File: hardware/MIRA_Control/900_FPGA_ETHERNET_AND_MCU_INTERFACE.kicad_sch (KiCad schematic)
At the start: 73 parts, among them J900 RJE71-188-1412, T900 H5007NLT, U500 XC7A200T-2FBG484I, U900 74LVC125APW, U901 74LVC125APW, U902 DP83867IRRGZR, U903 TLV75525PDBVR, U904 TPD2EUSB30DRTR, U905 TPD2EUSB30DRTR, U906 TPD2EUSB30DRTR, U907 TPD2EUSB30DRTR, Y900 ABM8-25.000MHZ-B2-T

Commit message: Add high-load schematic candidate with CORE sense and revised N15 supply
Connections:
- net VDD1P0 renamed PHY1V05
- net VDDA2P5 renamed PHY2V5
- net VDDIO renamed IO3V3

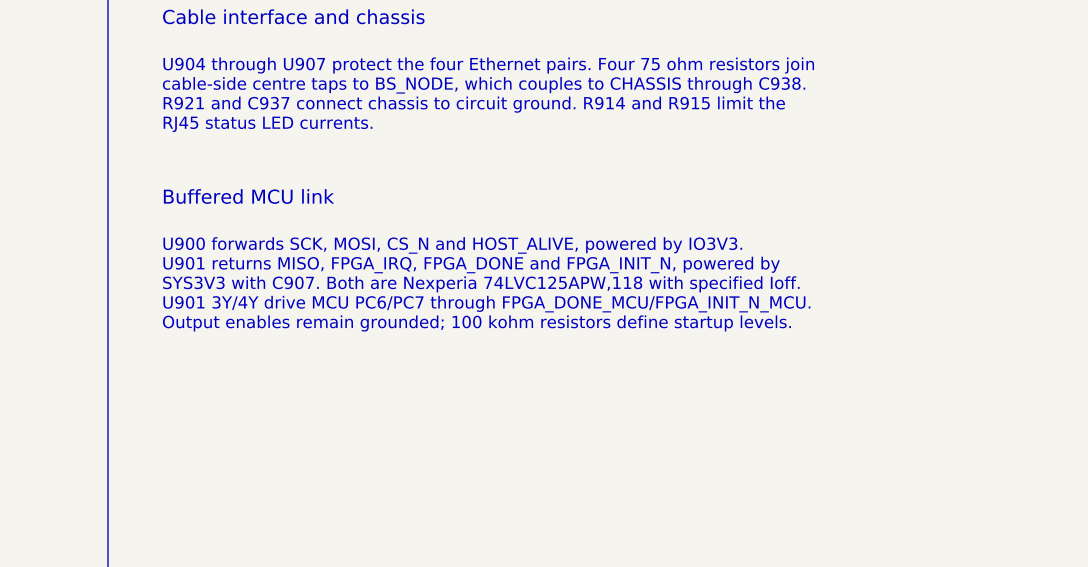
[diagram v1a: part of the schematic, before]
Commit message: Protect unpowered signal domains and qualify local supplies; retain startup and fault interlocks
MIRA-Startup-Patch: 7ffae17756ebcf923eff1212bb1aade8fbdfae03a9ca8ecebc69d3da3d3b4ba2
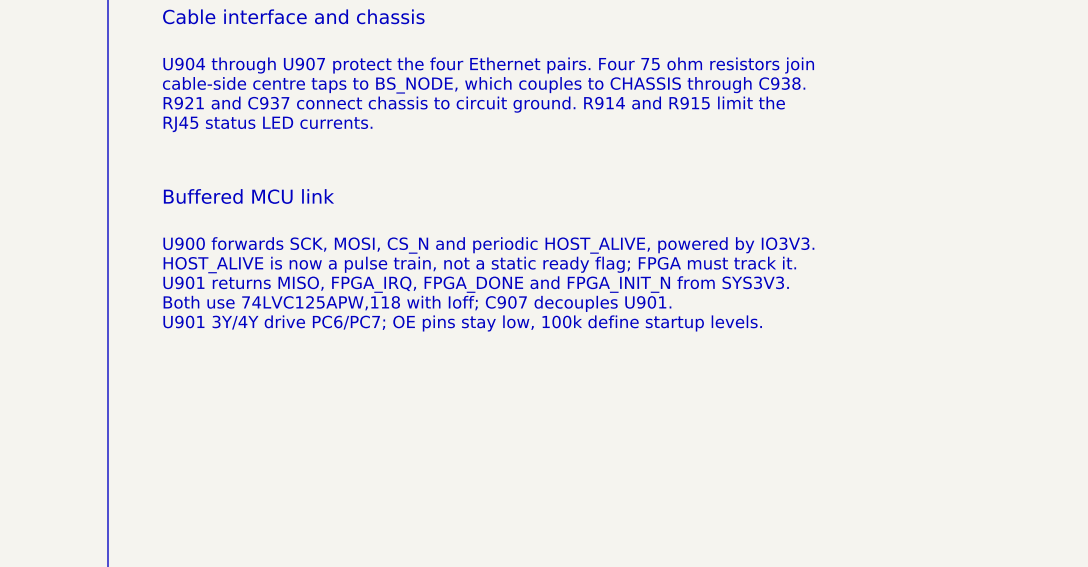
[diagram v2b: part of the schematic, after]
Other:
- note added: "U900 forwards SCK, MOSI, CS_N and periodic HOST_ALIVE, powered by IO3V3. HOST_ALIVE is now a pulse train, not a static ready flag; FPGA must track it. U901 returns MISO, FPGA_IRQ, FPGA_DONE and FPGA_INIT_N from SYS3V3. Both use 74LVC125APW,118 with Ioff; C907 decouples U901. U901 3Y/4Y drive PC6/PC7; OE pins stay low, 100k define startup levels."
- note removed: "U900 forwards SCK, MOSI, CS_N and HOST_ALIVE, powered by IO3V3. U901 returns MISO, FPGA_IRQ, FPGA_DONE and FPGA_INIT_N, powered by SYS3V3 with C907. Both are Nexperia 74LVC125APW,118 with specified Ioff. U901 3Y/4Y drive MCU PC6/PC7 through FPGA_DONE_MCU/FPGA_INIT_N_MCU. Output enables remain grounded; 100 kohm resistors define startup levels."
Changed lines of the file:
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@@
 		)
 	)
-	(text "U900 forwards SCK, MOSI, CS_N and HOST_ALIVE, powered by IO3V3.\nU901 returns MISO, FPGA_IRQ, FPGA_DONE and FPGA_INIT_N, powered by\nSYS3V3 with C907. Both are Nexperia 74LVC125APW,118 with specified Ioff.\nU901 3Y/4Y drive MCU PC6/PC7 through FPGA_DONE_MCU/FPGA_INIT_N_MCU.\nOutput enables remain grounded; 100 kohm resistors define startup levels."
+	(text "U900 forwards SCK, MOSI, CS_N and periodic HOST_ALIVE, powered by IO3V3.\nHOST_ALIVE is now a pulse train, not a static ready flag; FPGA must track it.\nU901 returns MISO, FPGA_IRQ, FPGA_DONE and FPGA_INIT_N from SYS3V3.\nBoth use 74LVC125APW,118 with Ioff; C907 decouples U901.\nU901 3Y/4Y drive PC6/PC7; OE pins stay low, 100k define startup levels."
 		(exclude_from_sim no)
 		(at 315 120.032 0)

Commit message: Verify digital pin maps and move MCU SPI clock to FPGA SRCC; prepare MIG inputs
MIRA-Digital-Patch: 73ac2f23a7d4a0d4119e0995085469fb50397bb688045691fe4033bcf7fa9ede
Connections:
- net MCU_FPGA_SCK_F: now also U500.Y11 (IO_L11P_T1_SRCC_13); no longer U500.AB12 (IO_L7N_T1_13)
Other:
- note added: "U900 forwards SCK, MOSI, CS_N and periodic HOST_ALIVE, powered by IO3V3. HOST_ALIVE is now a pulse train, not a static ready flag; FPGA must track it. U901 returns MISO, FPGA_IRQ, FPGA_DONE and FPGA_INIT_N from SYS3V3. Both use 74LVC125APW,118 with Ioff; C907 decouples U901. U901 3Y/4Y drive PC6/PC7; OE pins stay low, 100k define startup levels. SCK uses U500.Y11 (SRCC, bank 13); AB12 is unused. 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"
- note removed: "U900 forwards SCK, MOSI, CS_N and periodic HOST_ALIVE, powered by IO3V3. HOST_ALIVE is now a pulse train, not a static ready flag; FPGA must track it. U901 returns MISO, FPGA_IRQ, FPGA_DONE and FPGA_INIT_N from SYS3V3. Both use 74LVC125APW,118 with Ioff; C907 decouples U901. U901 3Y/4Y drive PC6/PC7; OE pins stay low, 100k define startup levels."
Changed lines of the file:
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@@
 		)
 	)
-	(text "U900 forwards SCK, MOSI, CS_N and periodic HOST_ALIVE, powered by IO3V3.\nHOST_ALIVE is now a pulse train, not a static ready flag; FPGA must track it.\nU901 returns MISO, FPGA_IRQ, FPGA_DONE and FPGA_INIT_N from SYS3V3.\nBoth use 74LVC125APW,118 with Ioff; C907 decouples U901.\nU901 3Y/4Y drive PC6/PC7; OE pins stay low, 100k define startup levels."
-		(exclude_from_sim no)
-		(at 315 120.032 0)
-		(effects
-			(font
-				(size 1.35 1.35)
-				(color 0 70 160 1)
-			)
-			(justify left top)
-		)
-	)
+	(text "U900 forwards SCK, MOSI, CS_N and periodic HOST_ALIVE, powered by IO3V3.\nHOST_ALIVE is now a pulse train, not a static ready flag; FPGA must track it.\nU901 returns MISO, FPGA_IRQ, FPGA_DONE and FPGA_INIT_N from SYS3V3.\nBoth use 74LVC125APW,118 with Ioff; C907 decouples U901.\nU901 3Y/4Y drive PC6/PC7; OE pins stay low, 100k define startup levels.\nSCK uses U500.Y11 (SRCC, bank 13); AB12 is unused. See digital-interfaces review." (exclude_from_sim no) (at 315 120.032 0) (effects (font (size 1.35 1.35) (color 0 70 160 1)) (justify left top)))
 	(text "Ethernet magnetics and center taps | Rev.A"
 		(exclude_from_sim no)
@@
 		(color 0 0 0 0)
 	)
-	(no_connect
-		(at 162.56 45.72)
-	)
+	(no_connect (at 116.84 72.39))
 	(no_connect
 		(at 254 45.72)
@@
 		)
 	)
-	(global_label "MCU_FPGA_SCK_F"
-		(shape bidirectional)
-		(at 116.84 72.39 180)
-		(effects
-			(font
-				(size 0.9 0.9)
-			)
-			(justify right)
-		)
-		(property "Intersheetrefs" "${INTERSHEET_REFS}"
-			(at 116.84 72.39 0)
-			(hide yes)
-			(show_name no)
-			(do_not_autoplace no)
-			(effects
-				(font
-					(size 1 1)
-				)
-			)
-		)
-	)
+	(global_label "MCU_FPGA_SCK_F" (shape bidirectional) (at 162.56 45.72 0) (effects (font (size 0.9 0.9)) (justify left)) (property "Intersheetrefs" "${INTERSHEET_REFS}" (at 162.56 45.72 0) (hide yes) (show_name no) (do_not_autoplace no) (effects (font (size 1 1)))))
 	(global_label "MDI_B_N"
 		(shape bidirectional)
